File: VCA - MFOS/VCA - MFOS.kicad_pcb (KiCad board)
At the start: 2 copper layers, 101.6 x 76.2 mm, 85 parts, among them J1 CVA1, J10 LINA, J11 OUTA, J12 CVB1, J13 CVB2, J14 Sig_In_B, J15 ADJB, J16 LOGB, J17 CMNB, J18 LINB, J19 OUTB, J2 CVA2, J3 Sig_In_A, J4 ADJA, J5 12V_Conn, J6 -12V_Conn, J7 Gnd_Conn, J8 LOGA, J9 CMNA, Q1 2N3904, Q2 2N3906, Q3 2N3904, Q4 2N3906, SW1 LOG_SW_A, SW2 LOG_SW_B, U1 TL084, U2 LM13700

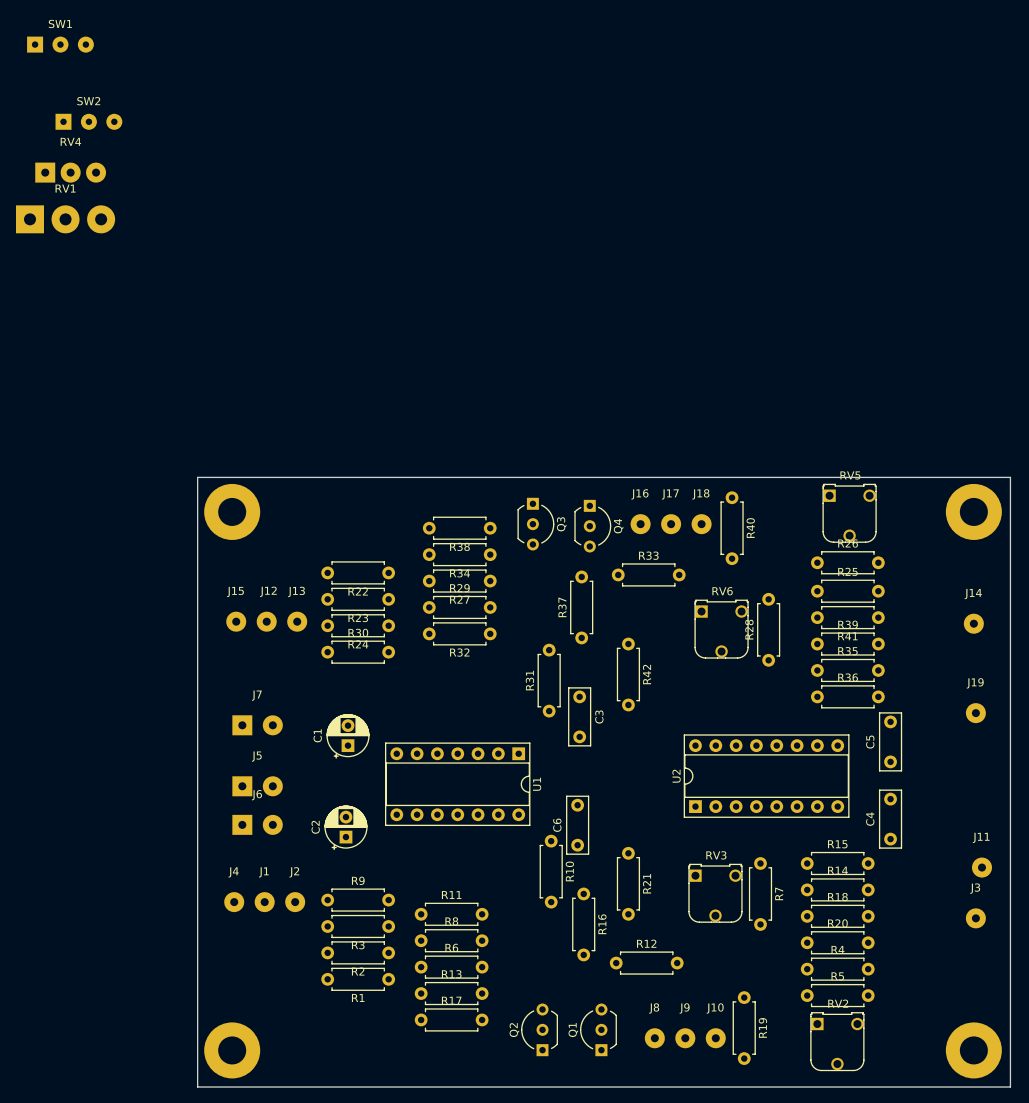
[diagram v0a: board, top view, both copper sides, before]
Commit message: pcb design for VCA finished
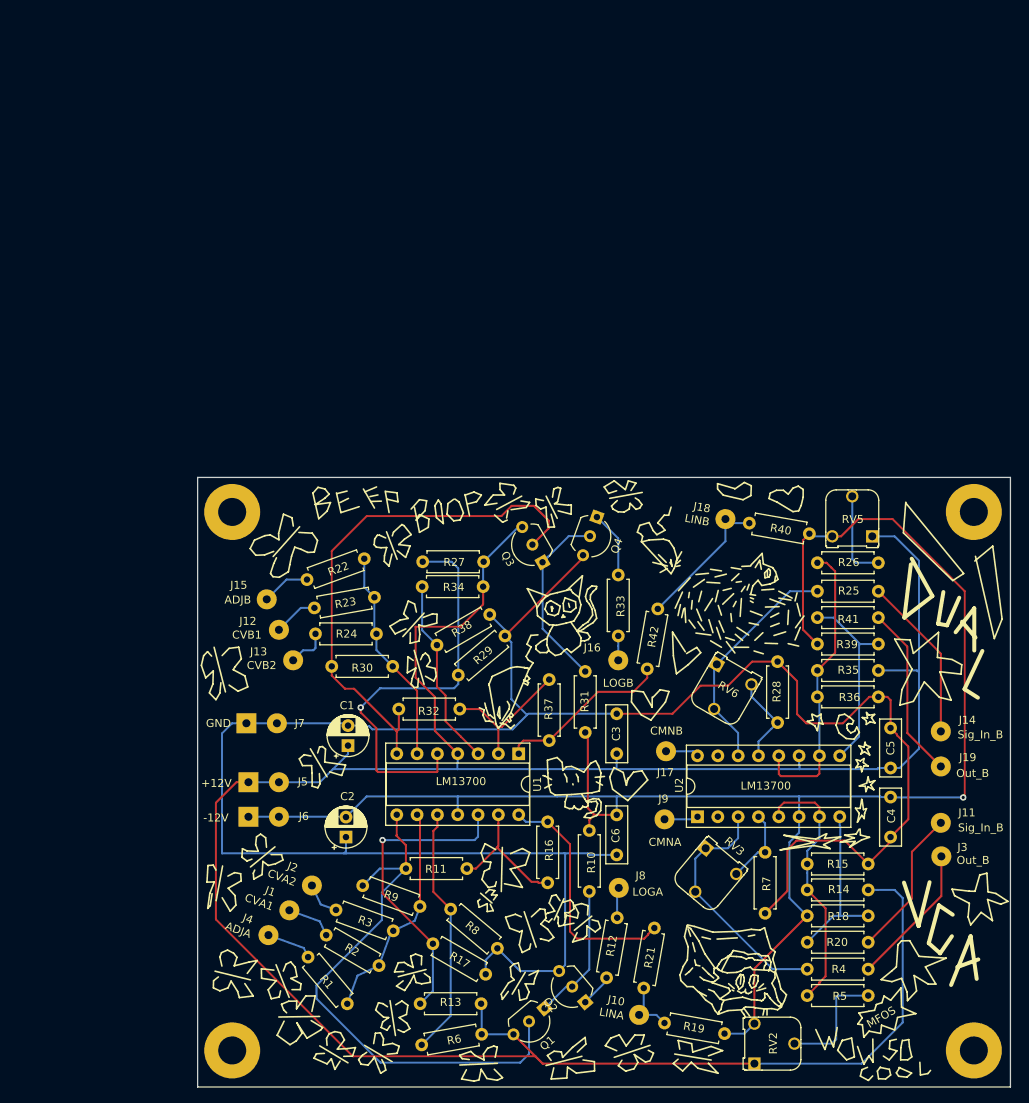
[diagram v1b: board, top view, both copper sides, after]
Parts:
- removed RV1: 100K, Connector_Wire:SolderWirePad_1x03_P4.445mm_Drill1.5mm
- removed RV4: 100K, Connector_Wire:SolderWirePad_1x03_P3.175mm_Drill1mm
- removed SW1: LOG_SW_A, Connector_Wire:SolderWirePad_1x03_P3.175mm_Drill0.8mm
- removed SW2: LOG_SW_B, Connector_Wire:SolderWirePad_1x03_P3.175mm_Drill0.8mm
- J5: value 12V_Conn -> +12V_Conn
- J7: value Gnd_Conn -> GND_Conn
- moved J17 28.4 mm to (70.7, 46.4)
- moved J9 27.5 mm to (70.5, 54.9)
- moved J8 19.3 mm to (64.8, 63.5)
- moved J16 17.2 mm to (64.8, 35.1)
- moved J14 14.1 mm to (105.1, 43.9)
- moved R37 13.5 mm to (56.1, 45.1)
- moved R38 10.8 mm to (48.7, 29.3), turned to 210 degrees
- moved R19 10.5 mm to (70.5, 80.4), turned to 350 degrees
- moved R32 10.1 mm to (45.0, 41.1)
- moved R29 10.1 mm to (50.6, 32.0), turned to 220 degrees
- moved R16 10.1 mm to (55.9, 55.2)
- moved J10 10.0 mm to (67.4, 79.4), turned to 350 degrees
- moved R17 9.88 mm to (48.2, 74.3), turned to 150 degrees
- moved R21 9.88 mm to (69.3, 68.5), turned to 260 degrees
- moved R6 9.72 mm to (40.2, 83.1), turned to 10 degrees
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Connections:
- J5 pad 2: (no net) -> +12V
- J6 pad 2: (no net) -> -12V
- J7 pad 2: (no net) -> Earth
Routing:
- net +12V: track 0.00 -> 318.8 mm
- net Earth: track 0.00 -> 263.2 mm
- net -12V: track 0.00 -> 213.0 mm, vias 0 -> 1
- net Net-(Q1-Pad2): track 0.00 -> 68.9 mm
- net Net-(Q3-Pad2): track 0.00 -> 66.3 mm
- net Net-(R27-Pad1): track 0.00 -> 51.3 mm, vias 0 -> 1
- net Net-(R13-Pad1): track 0.00 -> 38.6 mm, vias 0 -> 1
- net Net-(R26-Pad1): track 0.00 -> 36.6 mm
- net Net-(R14-Pad1): track 0.00 -> 32.8 mm
- net Net-(R6-Pad1): track 0.00 -> 31.4 mm
- net Net-(R4-Pad1): track 0.00 -> 31.2 mm
- net Net-(R16-Pad1): track 0.00 -> 30.4 mm
- net Net-(R25-Pad1): track 0.00 -> 29.2 mm
- net Net-(R1-Pad1): track 0.00 -> 28.0 mm
- net Net-(R22-Pad1): track 0.00 -> 27.1 mm
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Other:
- net class Default: clearance 0.2 -> 0.5
- rule trace_clearance: 0.2 -> 0.5
- rule via_min_size: 0.4 -> 0.6
- board text added: "+12V"
- board text added: "-12V"
- board text added: "ADJA"
- board text added: "ADJB"
- board text added: "CMNA"
- board text added: "CMNB"
- board text added: "CVA1"
- board text added: "CVA2"
- board text added: "CVB1"
- board text added: "CVB2"
- board text added: "GND"
- board text added: "LINA"
- board text added: "LINB"
- board text added: "LM13700"
- board text added: "LOGA"
- board text added: "LOGB"
- board text added: "MFOS"
- board text added: "Out_B"
- board text added: "Sig_In_B"

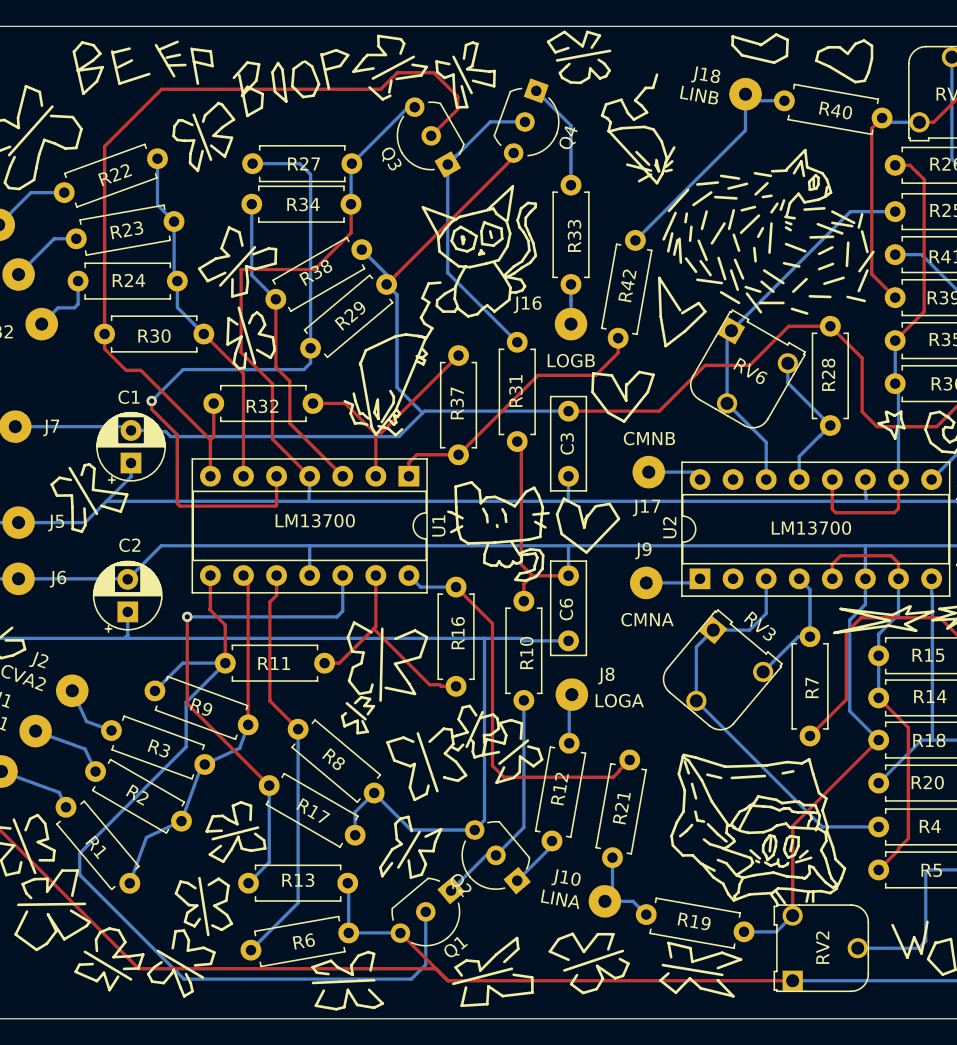
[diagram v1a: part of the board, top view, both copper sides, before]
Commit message: fixed transistor pinout on pcb
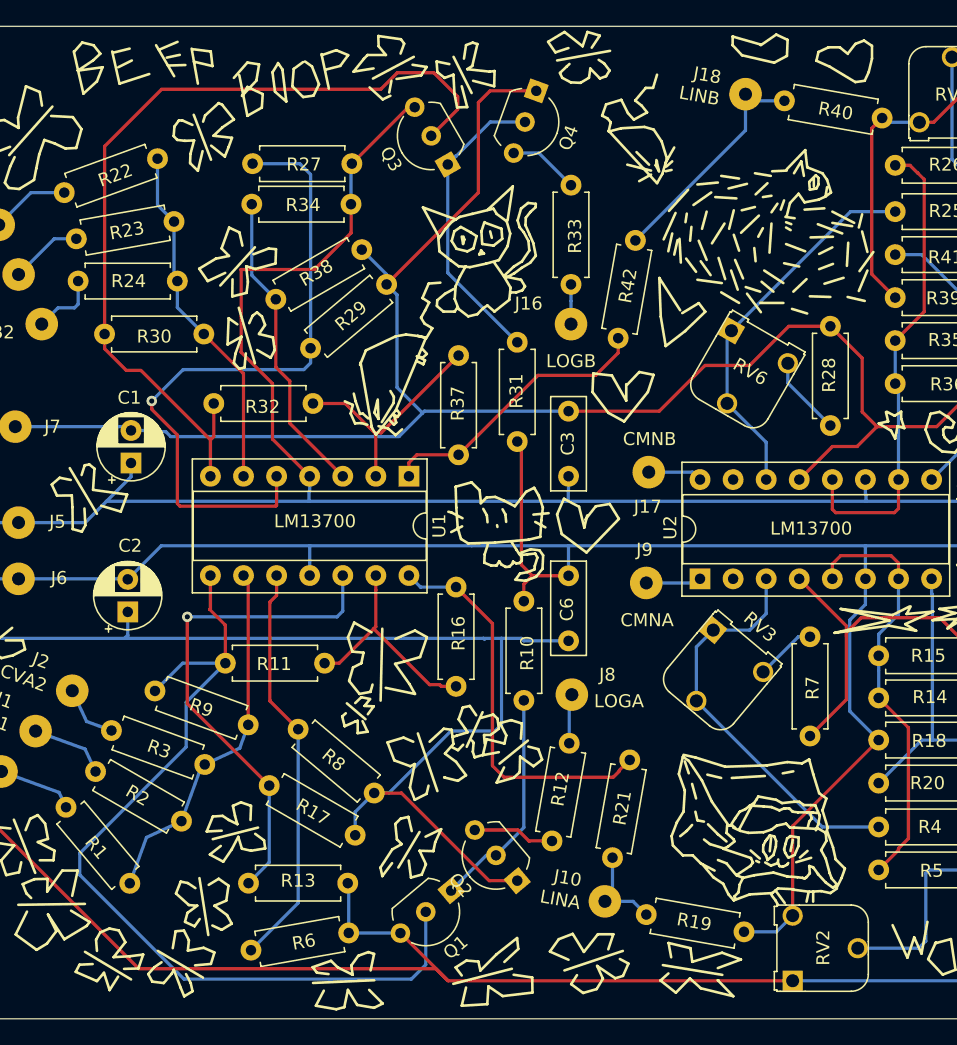
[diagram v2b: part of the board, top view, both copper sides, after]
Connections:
- Q2 pad 1: Net-(Q2-Pad1) -> Earth
- Q2 pad 3: Earth -> Net-(Q2-Pad3)
- Q4 pad 1: Net-(Q4-Pad1) -> Earth
- Q4 pad 3: Earth -> Net-(Q4-Pad3)
- R12 pad 1: Net-(Q2-Pad1) -> Net-(Q2-Pad3)
- R33 pad 1: Net-(Q4-Pad1) -> Net-(Q4-Pad3)
- U2 pad 13: Net-(R28-Pad1) -> Earth
- U2 pad 4: Net-(R7-Pad1) -> Earth
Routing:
- net Earth: track 263.2 -> 292.8 mm
- net Net-(Q4-Pad1): track 8.34 -> 0.00 mm
- net Net-(Q2-Pad3): track 0.00 -> 6.66 mm
- net Net-(Q4-Pad3): track 0.00 -> 5.75 mm
- net Net-(R28-Pad1): track 11.3 -> 6.13 mm
- net Net-(R7-Pad1): track 9.51 -> 4.72 mm
- net Net-(Q2-Pad1): track 4.15 -> 0.00 mm
- net Net-(Q3-Pad1): track 24.1 -> 23.2 mm

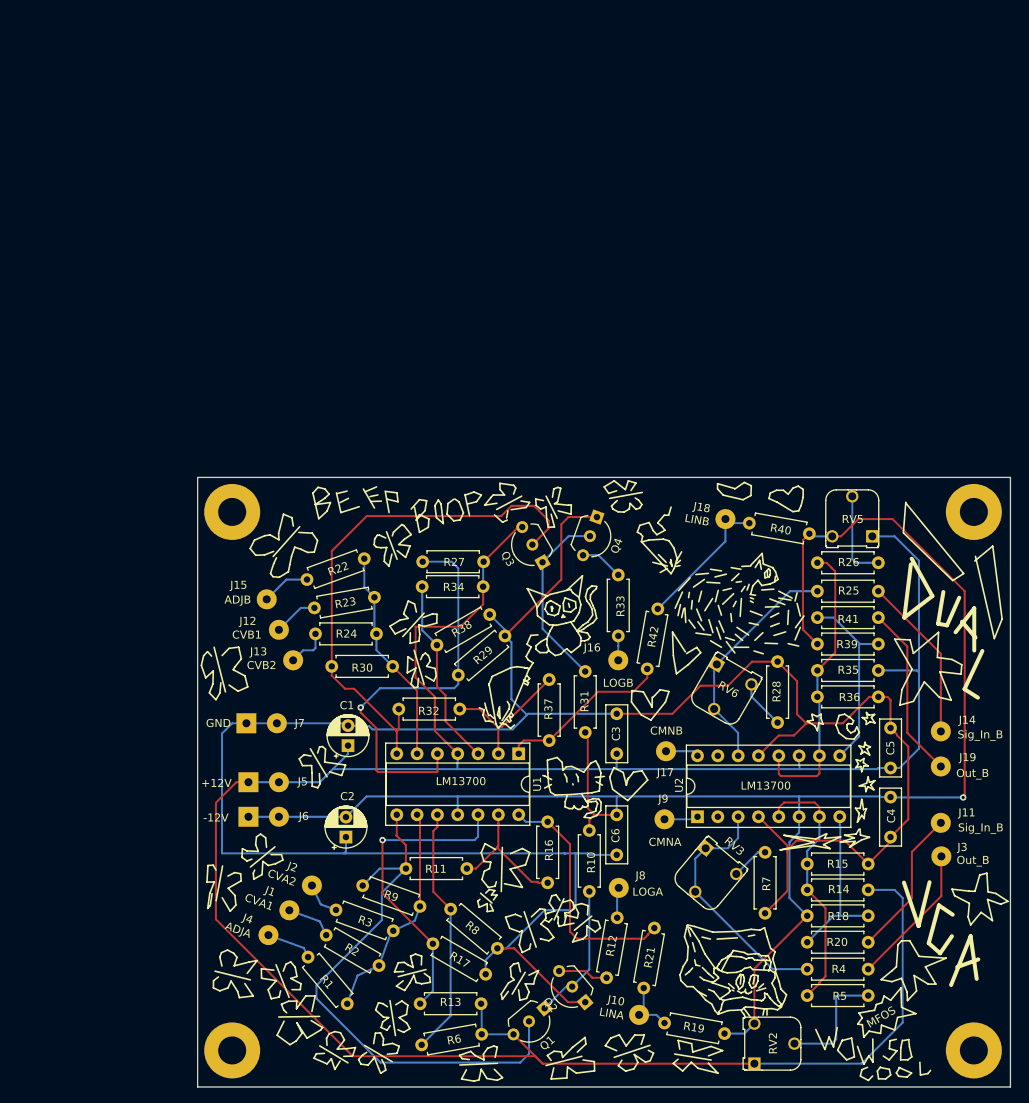
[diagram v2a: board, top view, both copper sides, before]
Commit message: added ground fills and vias to shorten ground paths
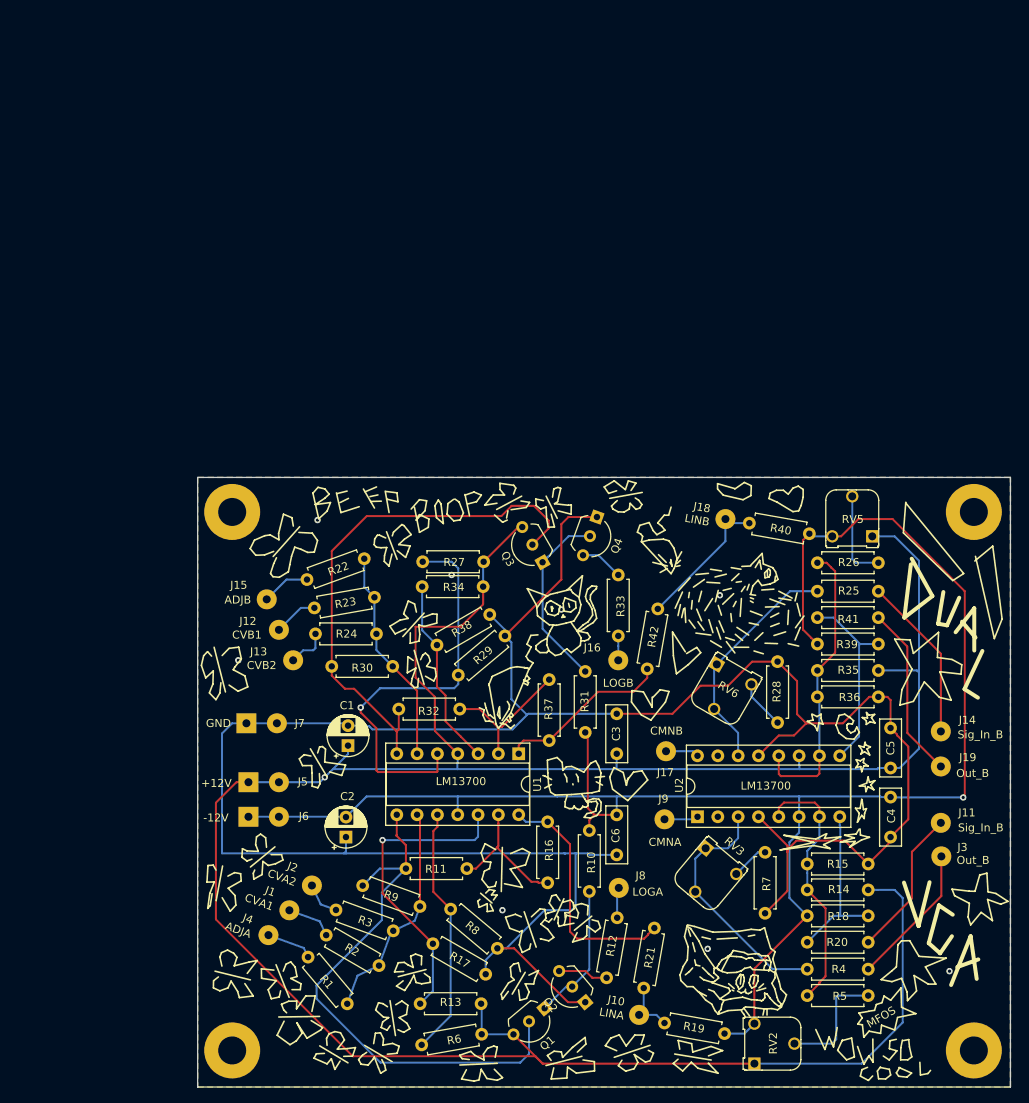
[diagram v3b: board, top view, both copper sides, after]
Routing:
- net Earth: vias 0 -> 8
- net +12V: vias 0 -> 1
- added copper zone on B.Cu, net Earth
- added copper zone on F.Cu, net Earth
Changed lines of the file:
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@@
     (thickness 1.6)
     (drawings 1356)
-    (tracks 426)
+    (tracks 436)
     (zones 0)
     (modules 81)
@@
   (segment (start 84.836 44.45) (end 86.741 44.45) (width 0.25) (layer F.Cu) (net 1))
   (segment (start 82.296 46.99) (end 84.836 44.45) (width 0.25) (layer F.Cu) (net 1))
+  (via (at 77.47 26.924) (size 0.8) (drill 0.4) (layers F.Cu B.Cu) (net 1))
+  (via (at 106.172 73.914) (size 0.8) (drill 0.4) (layers F.Cu B.Cu) (net 1))
+  (via (at 75.946 71.12) (size 0.8) (drill 0.4) (layers F.Cu B.Cu) (net 1))
+  (via (at 17.272 35.052) (size 0.8) (drill 0.4) (layers F.Cu B.Cu) (net 1))
+  (via (at 57.658 28.702) (size 0.8) (drill 0.4) (layers F.Cu B.Cu) (net 1))
+  (via (at 27.178 17.526) (size 0.8) (drill 0.4) (layers F.Cu B.Cu) (net 1))
+  (via (at 43.942 24.384) (size 0.8) (drill 0.4) (layers F.Cu B.Cu) (net 1))
+  (via (at 50.292 66.294) (size 0.8) (drill 0.4) (layers F.Cu B.Cu) (net 1))
   (segment (start 18.542 50.292) (end 22.352 50.292) (width 0.25) (layer B.Cu) (net 2))
   (segment (start 30.988 46.77) (end 30.988 45.72) (width 0.25) (layer B.Cu) (net 2))
   (segment (start 22.352 50.292) (end 27.466 50.292) (width 0.25) (layer B.Cu) (net 2))
-  (segment (start 27.466 50.292) (end 29.1 48.658) (width 0.25) (layer B.Cu) (net 2))
+  (segment (start 27.466 50.292) (end 28.084 49.674) (width 0.25) (layer B.Cu) (net 2))
   (segment (start 29.1 48.658) (end 30.988 46.77) (width 0.25) (layer B.Cu) (net 2))
   (segment (start 97.282 48.514) (end 98.806 48.514) (width 0.25) (layer B.Cu) (net 2))
@@
   (segment (start 47.9425 22.733) (end 52.278409 18.397091) (width 0.25) (layer F.Cu) (net 2))
   (segment (start 47.699735 81.798301) (end 51.654434 81.798301) (width 0.25) (layer B.Cu) (net 2))
+  (segment (start 28.084 49.674) (end 29.1 48.658) (width 0.25) (layer B.Cu) (net 2))
+  (via (at 28.084 49.674) (size 0.8) (drill 0.4) (layers F.Cu B.Cu) (net 2))
   (segment (start 18.542 54.61) (end 22.352 54.61) (width 0.25) (layer B.Cu) (net 3))
   (segment (start 30.694 54.61) (end 30.734 54.65) (width 0.25) (layer B.Cu) (net 3))
@@
   (segment (start 37.084 56.896) (end 37.084 54.356) (width 0.25) (layer F.Cu) (net 18))
   (segment (start 37.0205 56.9595) (end 37.084 56.896) (width 0.25) (layer F.Cu) (net 18))
-  (segment (start 35.221602 64.092398) (end 38.227 61.087) (width 0.25) (layer B.Cu) (net 18))
-  (segment (start 35.221602 67.521398) (end 35.221602 64.092398) (width 0.25) (layer B.Cu) (net 18))
-  (segment (start 27.051 75.692) (end 35.221602 67.521398) (width 0.25) (layer B.Cu) (net 18))
-  (segment (start 27.051 77.343) (end 27.051 75.692) (width 0.25) (layer B.Cu) (net 18))
-  (segment (start 52.5145 85.344) (end 35.052 85.344) (width 0.25) (layer B.Cu) (net 18))
-  (segment (start 35.052 85.344) (end 27.051 77.343) (width 0.25) (layer B.Cu) (net 18))
-  (segment (start 53.616747 84.241753) (end 52.5145 85.344) (width 0.25) (layer B.Cu) (net 18))
-  (segment (start 53.616747 80.182181) (end 53.616747 84.241753) (width 0.25) (layer B.Cu) (net 18))
+  (segment (start 52.5145 85.344) (end 53.616747 84.241753) (width 0.25) (layer B.Cu) (net 18))
+  (segment (start 27.051 75.692) (end 27.051 77.343) (width 0.25) (layer B.Cu) (net 18))
+  (segment (start 35.052 85.344) (end 52.5145 85.344) (width 0.25) (layer B.Cu) (net 18))
+  (segment (start 27.051 77.343) (end 35.052 85.344) (width 0.25) (layer B.Cu) (net 18))
+  (segment (start 35.221602 67.521398) (end 27.051 75.692) (width 0.25) (layer B.Cu) (net 18))
+  (segment (start 35.221602 64.092398) (end 35.221602 67.521398) (width 0.25) (layer B.Cu) (net 18))
+  (segment (start 38.227 61.087) (end 35.221602 64.092398) (width 0.25) (layer B.Cu) (net 18))
+  (segment (start 53.616747 84.241753) (end 53.616747 80.182181) (width 0.25) (layer B.Cu) (net 18))
   (segment (start 63.3095 75.1205) (end 63.3095 74.7395) (width 0.25) (layer B.Cu) (net 46))
   (segment (start 37.084 43.942) (end 37.084 46.736) (width 0.25) (layer F.Cu) (net 19))
@@
   (segment (start 62.304639 21.918639) (end 64.77 24.384) (width 0.25) (layer B.Cu) (net 47))
   (segment (start 60.365538 21.918639) (end 62.304639 21.918639) (width 0.25) (layer B.Cu) (net 47))
+  (zone (net 1) (net_name Earth) (layer B.Cu) (hatch edge 0.508)
+    (connect_pads (clearance 0.508))
+    (min_thickness 0.254)
+    (fill yes (arc_segments 32) (thermal_gap 0.508) (thermal_bridge_width 0.508))
+    (polygon
+      (pts
+        (xy 12.192 12.192) (xy 12.192 88.392) (xy 113.792 88.392) (xy 113.792 12.192)
+      )
+    )
+  )
+  (zone (net 1) (net_name Earth) (layer F.Cu) (hatch edge 0.508)
+    (connect_pads (clearance 0.508))
+    (min_thickness 0.254)
+    (fill yes (arc_segments 32) (thermal_gap 0.508) (thermal_bridge_width 0.508))
+    (polygon
+      (pts
+        (xy 12.192 12.192) (xy 12.192 88.392) (xy 113.792 88.392) (xy 113.792 12.192)
+      )
+    )
+  )
 )
